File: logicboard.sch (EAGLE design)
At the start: 16 parts, among them U1 RASPBERRY_PI_CM-1-1376408-4, X3 PCI-60-POS-145167, X4 PCI-60-POS-145167, X5 PCI-60-POS-145167

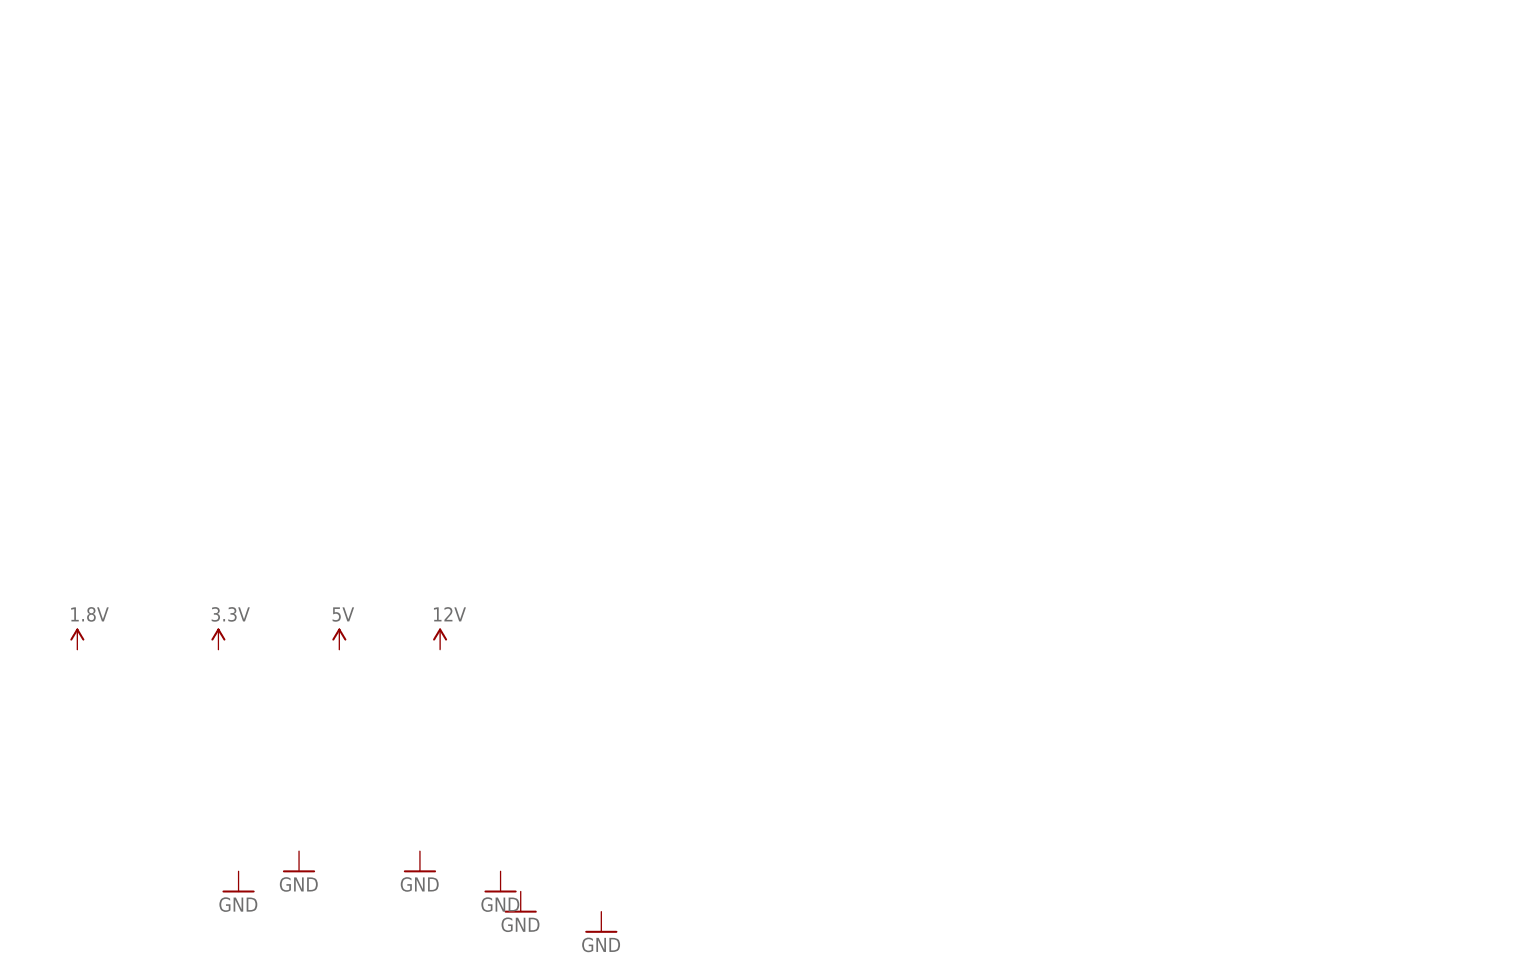
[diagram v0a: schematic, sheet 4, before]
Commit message: Initial schematic, missing USB, Ethernet, cheater HDMI jack
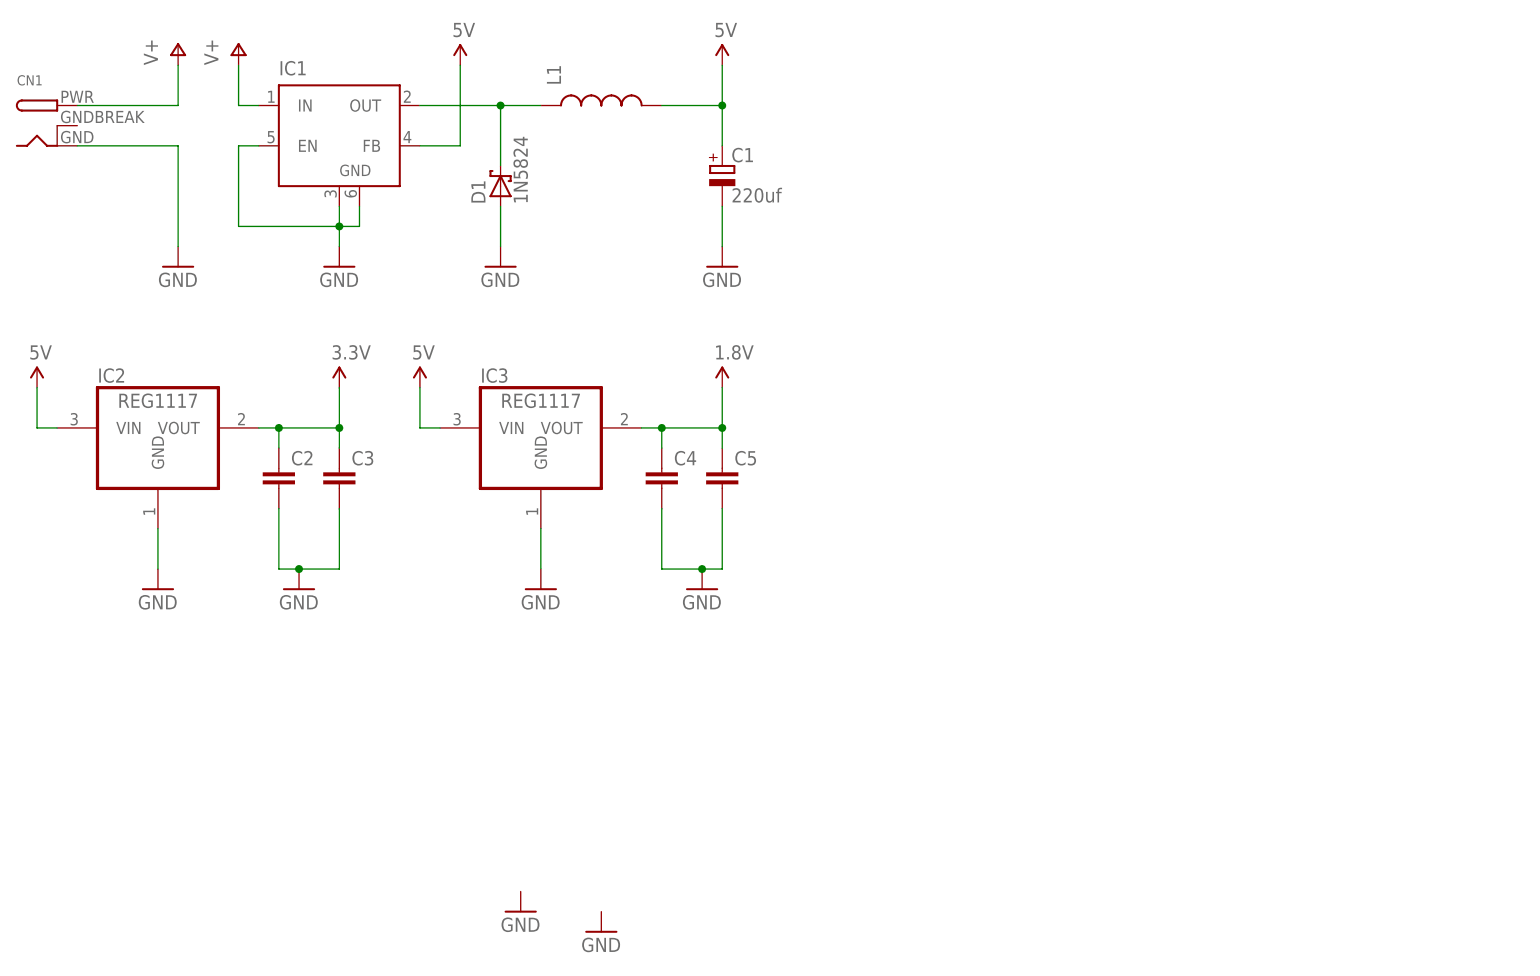
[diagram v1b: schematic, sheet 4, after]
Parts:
- removed SERIAL2: (no value), con-subd:F09HP
- added C1: 220uf, rcl:CPOL-EUE2.5-6
- added C2, C3, C4, C5: (no value), SparkFun-Capacitors:CAP1206
- added CN1: (no value), adafruit:DCBARRELPTH
- added D1: 1N5824, diode:1N5817-B
- added IC1: (no value), linear:LM2596S
- added IC2, IC3: REG1117, burr-brown:REG1117
- added L1: (no value), SparkFun-Passives:INDUCTORSRU1038
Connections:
- new net V+: CN1.PWR, IC1.IN
- new net VOUT: D1.C, IC1.OUT, L1.1
- net 1.8V: now also C4.1, C5.1, IC3.VOUT
- net 3.3V: now also C2.1, C3.1, IC2.VOUT
- net 5V: now also C1.+, IC1.FB, IC2.VIN, IC3.VIN, L1.2
- net GND: now also C1.-, C2.2, C3.2, C4.2, C5.2, CN1.GND, D1.A, IC1.EN, IC1.GND, IC1.GND@1, IC2.GND, IC3.GND

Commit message: Initial commit
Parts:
- removed JP1: (no value), SparkFun-Connectors:M05X2SHD_LOCK
- removed X3, X4, X5: PCI-60-POS-145167, con-amp:PCI-60-POS-145167
- added AUDIO: (no value), SparkFun-Connectors:AUDIO-JACKPTH
- added C10, C13: 0.01uf, SparkFun-Capacitors:CAPEZ
- added C11, C14: 100uf, SparkFun-Capacitors:CAPEZ
- added C12, C15: 0.001uf, SparkFun-Capacitors:CAPEZ
- added C16, C17: (no value), SparkFun-Capacitors:CAP1206
- added C6, C7: 10uf, SparkFun-Capacitors:CAPEZ
- added C8, C9: 33n, SparkFun-Capacitors:CAPEZ
- added CHEATER: (no value), SparkFun-Connectors:M08X2
- added EXP1, EXP2, EXP3, EXP4, EXP5, EXP6, VIDEOCORE_JTAG: (no value), SparkFun-Connectors:M05X2SHD_LOCK
- added H1, H2, H3, H4, H5, H6, H7, H8: MOUNT-HOLE4.5, holes:MOUNT-HOLE4.5
- added IC4: MCP2300X/P, adafruit:MCP2300X/P
- added IC5: REG1117, burr-brown:REG1117
- added PWR_SWITCH: (no value), SparkFun-Connectors:M02POLAR
- added Q2: MOSFET-NCHANNELBS170, SparkFun-DiscreteSemi:MOSFET-NCHANNELBS170
- added R1, R2: 10k, SparkFun-Resistors:10KOHM-1/4W-1%(PTH)HORIZ-KIT
- added R3, R4: 150r, SparkFun-Resistors:RESISTOREZ
- added R5, R6: 270R, SparkFun-Resistors:RESISTOREZ
- added R7: (no value), SparkFun-Resistors:RPACK-BUSSED-8-SIP-PTH-8
- added R8, R9: (no value), SparkFun-Resistors:RESISTOREZ
- added SERIAL1_PORTFLIP, USB_POLARITY: FEMALE 2x3, SparkFun-Connectors:M03X2FEMALE
- added SPKR_L, SPKR_R: (no value), SparkFun-Connectors:M02JST-PTH-2-KIT
- added U$1, U$2: TDA7052, tda7052:TDA7052
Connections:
- new net AUDIO_GROUND: C12.2, C15.2, Q2.D, U$1.GND, U$1.SG, U$2.GND, U$2.SG
- new net CPU_3.3V: C16.1, C17.1, IC5.VOUT, U1_PWR.3V3, U1_PWR.VBAT, U1_PWR.VDAC
- new net CTS: SERIAL1.8
- new net DCD: SERIAL1.1
- new net DSR: SERIAL1.6
- new net DTR: SERIAL1.4
- new net HDMI_CEC: CHEATER.15, U1_HDMI.HDMI_CEC
- new net HDMI_CK_N: CHEATER.2, U1_HDMI.HDMI_CK_N
- new net HDMI_CK_P: CHEATER.4, U1_HDMI.HDMI_CK_P
- new net HDMI_D0_N: CHEATER.6, U1_HDMI.HDMI_D0_N
- new net HDMI_D0_P: CHEATER.8, U1_HDMI.HDMI_D0_P
- new net HDMI_D1_N: CHEATER.10, U1_HDMI.HDMI_D1_N
- new net HDMI_D1_P: CHEATER.12, U1_HDMI.HDMI_D1_P
- new net HDMI_D2_N: CHEATER.14, U1_HDMI.HDMI_D2_N
- new net HDMI_D2_P: CHEATER.16, U1_HDMI.HDMI_D2_P
- new net HDMI_SCL: CHEATER.7, U1_HDMI.HDMI_SCL
- new net HDMI_SDA: CHEATER.11, U1_HDMI.HDMI_SDA
- new net IO_RST: IC4./RST, R9.2
- new net LOUT_L: AUDIO.LEFT, C12.1, C7.2, U$1.INPUT
- new net LOUT_R: AUDIO.RIGHT, C15.1, C6.2, U$2.INPUT
- new net N$10: SPKR_L.2, U$1.OUT1
- new net N$11: SPKR_L.1, U$1.OUT2
- new net N$12: Q2.G, R8.2
- new net N$14: IC4.INT
- new net N$16: IC4.GP5, R7.7
- new net N$17: IC4.GP4, R7.6
- new net N$18: IC4.GP3, R7.5
- new net N$19: IC4.GP2, R7.4
- new net N$20: IC4.GP1, R7.3
- new net N$21: IC4.GP0, R7.2
- new net N$22: SPKR_R.2, U$2.OUT1
- new net N$23: SPKR_R.1, U$2.OUT2
- new net N$7: U1_RUN.EMMC_DISABLE_N
- new net N$8: CN1.PWR, PWR_SWITCH.1
- new net N$9: U1_USB.USB_OTGID
- new net NC: EXP5.6
- new net PORT_RX: SERIAL1.2, SERIAL1_PORTFLIP.3
- new net PORT_TX: SERIAL1.3, SERIAL1_PORTFLIP.4
- new net PWM0_R: C6.1, C8.1, R3.2, R5.2
- new net PWM1_L: C7.1, C9.1, R4.2, R6.2
- new net RI: SERIAL1.9
- new net RTS: SERIAL1.7
- new net RUN: U1_RUN.RUN
- new net SPKR_ENABLE: IC4.GP7, R7.9, R8.1
- new net USB+: EXP5.10, USB_POLARITY.1, USB_POLARITY.6
- new net USB-: EXP5.9, USB_POLARITY.2, USB_POLARITY.5
- new net USB_D+: U1_USB.USB_DP_P, USB_POLARITY.3
- new net USB_D-: U1_USB.USB_DM_N, USB_POLARITY.4
- net 3.3V: now also EXP6.5, EXP6.6, IC4.VCC, R1.2, R2.2, R9.1; no longer EXT_I2C_1.1, EXT_I2C_1.2, EXT_I2C_2.1, EXT_I2C_2.2, U1_PWR.3V3, X3-1.1, X3-2.1, X3-3.1, X3-4.1, X3-5.1, X3-6.1, X3-7.1, X3-8.1, X4-1.1, X4-2.1, X4-3.1, X4-4.1, X4-5.1, X4-6.1, X4-7.1, X4-8.1, X5-1.1, X5-2.1, X5-3.1, X5-4.1, X5-5.1, X5-6.1, X5-7.1, X5-8.1
- net 5V: now also C10.1, C11.1, C13.1, C14.1, EXP6.3, EXP6.4, EXT_I2C_1.1, EXT_I2C_1.2, EXT_I2C_2.1, EXT_I2C_2.2, IC5.VIN, U$1.VP, U$2.VP; no longer X3-17.1, X3-18.1, X3-19.1, X3-20.1, X3-21.1, X3-22.1, X3-23.1, X3-24.1, X4-17.1, X4-18.1, X4-19.1, X4-20.1, X4-21.1, X4-22.1, X4-23.1, X4-24.1, X5-17.1, X5-18.1, X5-19.1, X5-20.1, X5-21.1, X5-22.1, X5-23.1, X5-24.1
- net GND: now also AUDIO.SLEEVE, C10.2, C11.2, C13.2, C14.2, C16.2, C17.2, C8.2, C9.2, CHEATER.1, CHEATER.13, CHEATER.3, CHEATER.5, CHEATER.9, EXP5.7, EXP5.8, EXP6.1, EXP6.2, EXP6.7, EXP6.8, IC4.A0, IC4.A1, IC4.A2, IC4.GND, IC5.GND, Q2.S, R3.1, R4.1, R7.1, SERIAL1.5, VIDEOCORE_JTAG.10, VIDEOCORE_JTAG.2, VIDEOCORE_JTAG.4, VIDEOCORE_JTAG.6, VIDEOCORE_JTAG.8; no longer JP1.10, JP1.2, JP1.4, JP1.6, JP1.8, X3-10.1, X3-11.1, X3-12.1, X3-13.1, X3-14.1, X3-15.1, X3-16.1, X3-9.1, X4-10.1, X4-11.1, X4-12.1, X4-13.1, X4-14.1, X4-15.1, X4-16.1, X4-9.1, X5-10.1, X5-11.1, X5-12.1, X5-13.1, X5-14.1, X5-15.1, X5-16.1, X5-9.1
- net GPIO10: now also EXP2.1; no longer X3-45.1, X3-46.1, X4-45.1, X4-46.1, X5-45.1, X5-46.1
- net GPIO11: now also EXP2.2; no longer X3-47.1, X3-48.1, X4-47.1, X4-48.1, X5-47.1, X5-48.1
- net GPIO12: now also EXP2.3; no longer X3-49.1, X3-50.1, X4-49.1, X4-50.1, X5-49.1, X5-50.1
- net GPIO13: now also EXP2.4; no longer X3-51.1, X3-52.1, X4-51.1, X4-52.1, X5-51.1, X5-52.1
- net GPIO17: now also EXP2.7; no longer X3-57.1, X3-58.1, X4-57.1, X4-58.1, X5-57.1, X5-58.1
- net GPIO18: now also EXP2.8; no longer X3-59.1, X3-60.1, X4-59.1, X4-60.1, X5-59.1, X5-60.1
- net GPIO19: now also EXP2.9; no longer X3-61.1, X3-62.1, X4-61.1, X4-62.1, X5-61.1, X5-62.1
- net GPIO20: now also EXP2.10; no longer X3-63.1, X3-64.1, X4-63.1, X4-64.1, X5-63.1, X5-64.1
- net GPIO21: now also EXP3.1; no longer X3-65.1, X3-66.1, X4-65.1, X4-66.1, X5-65.1, X5-66.1
- net GPIO22: now also EXP3.2; no longer X3-67.1, X3-68.1, X4-67.1, X4-68.1, X5-67.1, X5-68.1
- net GPIO23: now also EXP3.3; no longer X3-69.1, X3-70.1, X4-69.1, X4-70.1, X5-69.1, X5-70.1
- net GPIO24: now also EXP3.4; no longer X3-71.1, X3-72.1, X4-71.1, X4-72.1, X5-71.1, X5-72.1
- net GPIO25: now also EXP3.5; no longer X3-73.1, X3-74.1, X4-73.1, X4-74.1, X5-73.1, X5-74.1
- net GPIO26: now also EXP3.6; no longer X3-75.1, X3-76.1, X4-75.1, X4-76.1, X5-75.1, X5-76.1
- net GPIO27: now also EXP3.7; no longer X3-77.1, X3-78.1, X4-77.1, X4-78.1, X5-77.1, X5-78.1
- net GPIO28: now also EXP3.8; no longer X3-79.1, X3-80.1, X4-79.1, X4-80.1, X5-79.1, X5-80.1
- net GPIO29: now also EXP3.9; no longer X3-81.1, X3-82.1, X4-81.1, X4-82.1, X5-81.1, X5-82.1
- net GPIO30: now also EXP3.10; no longer X3-83.1, X3-84.1, X4-83.1, X4-84.1, X5-83.1, X5-84.1
- net GPIO31: now also EXP4.1; no longer X3-85.1, X3-86.1, X4-85.1, X4-86.1, X5-85.1, X5-86.1
- net GPIO32: now also EXP4.2; no longer X3-87.1, X3-88.1, X4-87.1, X4-88.1, X5-87.1, X5-88.1
- net GPIO33: now also EXP4.3; no longer X3-89.1, X3-90.1, X4-89.1, X4-90.1, X5-89.1, X5-90.1
- net GPIO34: now also EXP4.4; no longer X3-91.1, X3-92.1, X4-91.1, X4-92.1, X5-91.1, X5-92.1
- net GPIO35: now also EXP4.5; no longer X3-93.1, X3-94.1, X4-93.1, X4-94.1, X5-93.1, X5-94.1
- net GPIO36: now also EXP4.6; no longer X3-95.1, X3-96.1, X4-95.1, X4-96.1, X5-95.1, X5-96.1
- net GPIO37: now also EXP4.7; no longer X3-97.1, X3-98.1, X4-97.1, X4-98.1, X5-97.1, X5-98.1
- net GPIO38: now also EXP4.8; no longer X3-100.1, X3-99.1, X4-100.1, X4-99.1, X5-100.1, X5-99.1
- net GPIO39: now also EXP4.9; no longer X3-101.1, X3-102.1, X4-101.1, X4-102.1, X5-101.1, X5-102.1
- net GPIO4: now also EXP1.5; no longer X3-33.1, X3-34.1, X4-33.1, X4-34.1, X5-33.1, X5-34.1
- net GPIO40: now also EXP4.10, R5.1; no longer X3-103.1, X3-104.1, X4-103.1, X4-104.1, X5-103.1, X5-104.1
- net GPIO41: now also EXP5.1, R6.1; no longer X3-105.1, X3-106.1, X4-105.1, X4-106.1, X5-105.1, X5-106.1
- net GPIO42: now also EXP5.2; no longer X3-107.1, X3-108.1, X4-107.1, X4-108.1, X5-107.1, X5-108.1
- net GPIO43: now also EXP5.3; no longer X3-109.1, X3-110.1, X4-109.1, X4-110.1, X5-109.1, X5-110.1
- net GPIO44: now also EXP5.4; no longer X3-111.1, X3-112.1, X4-111.1, X4-112.1, X5-111.1, X5-112.1
- net GPIO45: now also EXP5.5; no longer X3-113.1, X3-114.1, X4-113.1, X4-114.1, X5-113.1, X5-114.1
- net GPIO5: now also EXP1.6; no longer X3-35.1, X3-36.1, X4-35.1, X4-36.1, X5-35.1, X5-36.1
- net GPIO6: now also EXP1.7; no longer X3-37.1, X3-38.1, X4-37.1, X4-38.1, X5-37.1, X5-38.1
- net GPIO7: now also EXP1.8; no longer X3-39.1, X3-40.1, X4-39.1, X4-40.1, X5-39.1, X5-40.1
- net GPIO8: now also EXP1.9; no longer X3-41.1, X3-42.1, X4-41.1, X4-42.1, X5-41.1, X5-42.1
- net GPIO9: now also EXP1.10; no longer X3-43.1, X3-44.1, X4-43.1, X4-44.1, X5-43.1, X5-44.1
- net LED_NOTIFICATION: now also IC4.GP6, R7.8
- net N$1: now also VIDEOCORE_JTAG.9; no longer JP1.9
- net N$2: now also VIDEOCORE_JTAG.7; no longer JP1.7
- net N$3: now also VIDEOCORE_JTAG.5; no longer JP1.5
- net N$4: now also VIDEOCORE_JTAG.3; no longer JP1.3
- net N$5: now also VIDEOCORE_JTAG.1; no longer JP1.1
- net RXD0: now also EXP2.6, SERIAL1_PORTFLIP.1, SERIAL1_PORTFLIP.6; no longer X3-55.1, X3-56.1, X4-55.1, X4-56.1, X5-55.1, X5-56.1
- net SCL: now also EXP1.2, IC4.SCL, R1.1; no longer X3-27.1, X3-28.1, X4-27.1, X4-28.1, X5-27.1, X5-28.1
- net SCL1: now also EXP1.4; no longer X3-31.1, X3-32.1, X4-31.1, X4-32.1, X5-31.1, X5-32.1
- net SDA: now also EXP1.1, IC4.SDA, R2.1; no longer X3-25.1, X3-26.1, X4-25.1, X4-26.1, X5-25.1, X5-26.1
- net SDA1: now also EXP1.3; no longer X3-29.1, X3-30.1, X4-29.1, X4-30.1, X5-29.1, X5-30.1
- net TXD0: now also EXP2.5, SERIAL1_PORTFLIP.2, SERIAL1_PORTFLIP.5; no longer X3-53.1, X3-54.1, X4-53.1, X4-54.1, X5-53.1, X5-54.1
- net V+: now also EXP6.10, EXP6.9, PWR_SWITCH.2; no longer CN1.PWR
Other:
- note added: "May want to revisit and give the core a dedicated 3.3v service"

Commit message: for now, a complete logic board and expansion board until I find something wrong with it
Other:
- moved on the sheet: U1_PWR
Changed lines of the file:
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@@
 </plain>
 <instances>
-<instance part="U1" gate="_PWR" x="20.32" y="147.32"/>
+<instance part="U1" gate="_PWR" x="17.78" y="147.32"/>
 <instance part="U1" gate="_RUN" x="93.98" y="165.1"/>
 <instance part="U1" gate="_USB" x="17.78" y="58.42"/>
@@
 <pinref part="U1" gate="_PWR" pin="GND"/>
 <pinref part="GND17" gate="1" pin="GND"/>
-<wire x1="33.02" y1="139.7" x2="63.5" y2="139.7" width="0.1524" layer="91"/>
+<wire x1="30.48" y1="139.7" x2="63.5" y2="139.7" width="0.1524" layer="91"/>
 <wire x1="63.5" y1="139.7" x2="63.5" y2="137.16" width="0.1524" layer="91"/>
 </segment>
@@
 <segment>
 <pinref part="U1" gate="_PWR" pin="1V8"/>
-<wire x1="33.02" y1="157.48" x2="35.56" y2="157.48" width="0.1524" layer="91"/>
+<wire x1="30.48" y1="157.48" x2="35.56" y2="157.48" width="0.1524" layer="91"/>
 <pinref part="SUPPLY14" gate="G$1" pin="1.8V"/>
 <wire x1="35.56" y1="157.48" x2="35.56" y2="160.02" width="0.1524" layer="91"/>
@@
 <segment>
 <pinref part="U1" gate="_PWR" pin="3V3"/>
-<wire x1="33.02" y1="154.94" x2="43.18" y2="154.94" width="0.1524" layer="91"/>
+<wire x1="30.48" y1="154.94" x2="43.18" y2="154.94" width="0.1524" layer="91"/>
 <pinref part="U1" gate="_PWR" pin="VBAT"/>
-<wire x1="33.02" y1="149.86" x2="43.18" y2="149.86" width="0.1524" layer="91"/>
+<wire x1="30.48" y1="149.86" x2="43.18" y2="149.86" width="0.1524" layer="91"/>
 <wire x1="43.18" y1="149.86" x2="43.18" y2="152.4" width="0.1524" layer="91"/>
 <pinref part="U1" gate="_PWR" pin="VDAC"/>
 <wire x1="43.18" y1="152.4" x2="43.18" y2="154.94" width="0.1524" layer="91"/>
-<wire x1="33.02" y1="152.4" x2="43.18" y2="152.4" width="0.1524" layer="91"/>
+<wire x1="30.48" y1="152.4" x2="43.18" y2="152.4" width="0.1524" layer="91"/>
 <junction x="43.18" y="152.4"/>
 <junction x="43.18" y="154.94"/>
